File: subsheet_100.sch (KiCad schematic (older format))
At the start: 21 parts, among them U100 MC68000_PLCC_68_PHY, U100_DIP64 MC68000_DIP_64_SOCKET

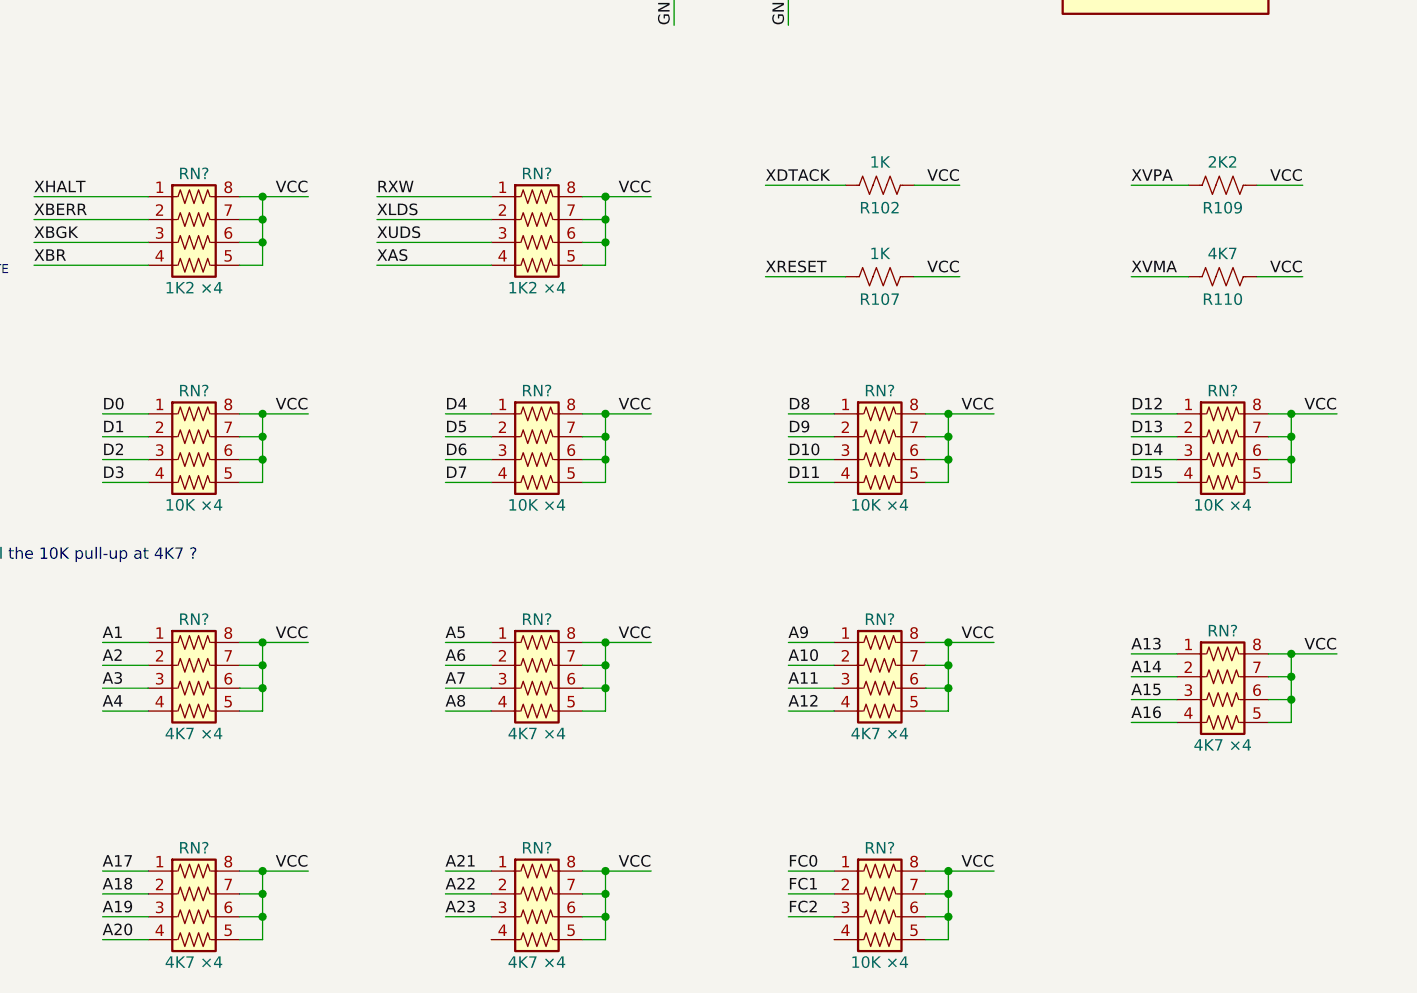
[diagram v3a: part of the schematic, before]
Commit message: annotate resistor networks and mark unused pins as unconnected
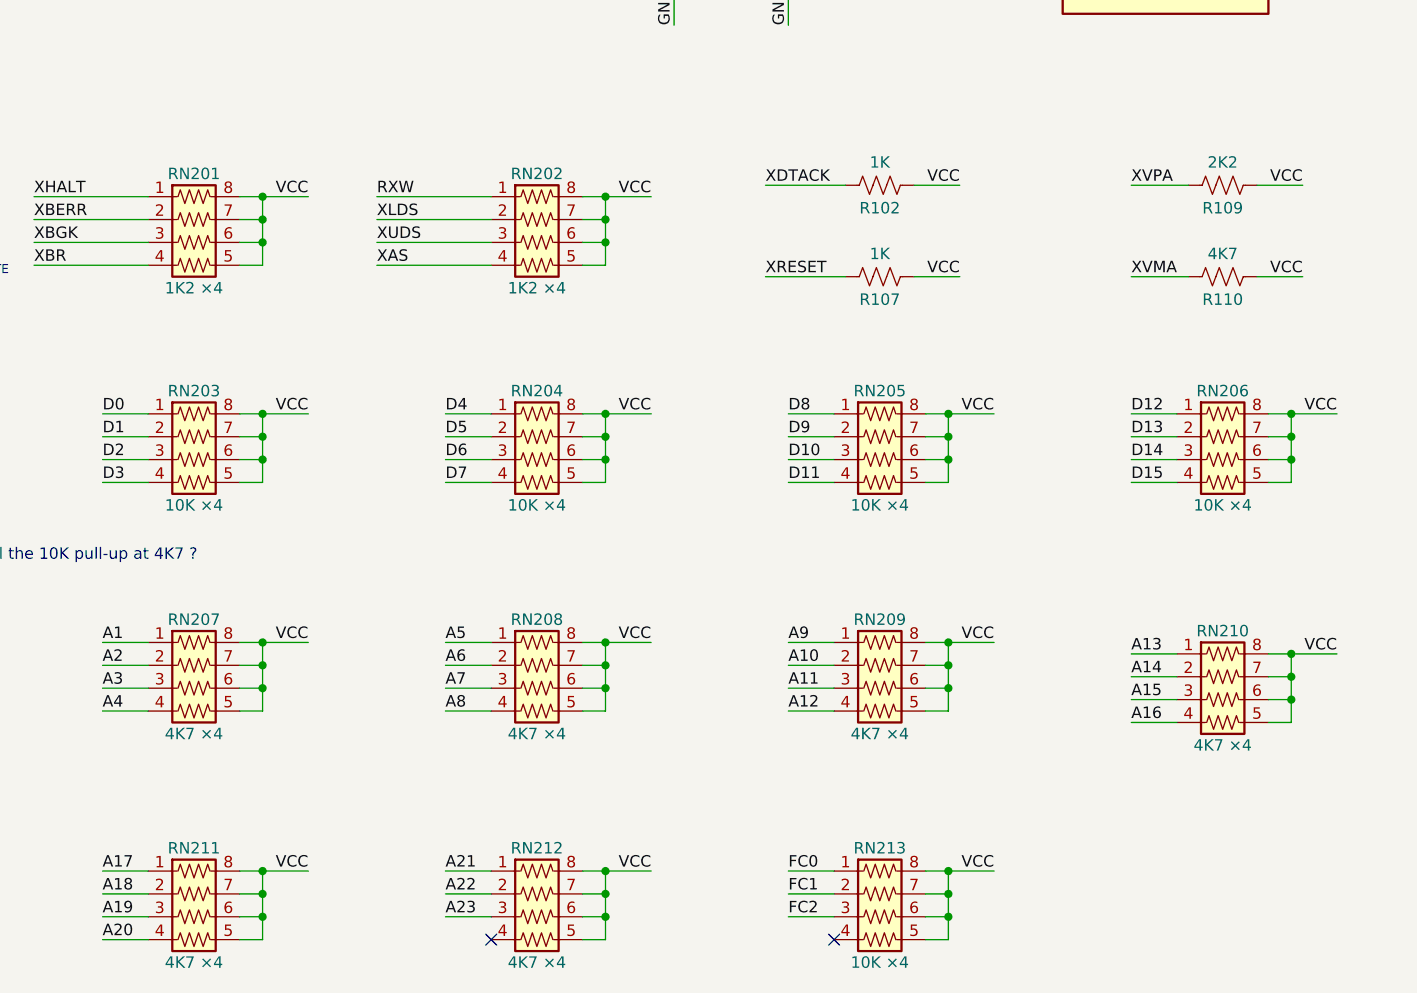
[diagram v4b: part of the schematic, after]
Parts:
- gave numbers to parts that had none: 13
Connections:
- no-connect marks 0 -> 2
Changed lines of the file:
@@
 XBGK when coming to \nBlitter is pulled-up\nwith 4K7, but in my STE\nit was not populated \nanyway (no external\nBlitter), so pulled-up \nwith 1K2 should be ok
 $Comp
-L custom_passives:R_Pack04_US RN?
+L custom_passives:R_Pack04_US RN201
 U 1 1 61B5A520
 P 2000 6250
-F 0 "RN?" V 1700 6250 50  0000 C CNN
+F 0 "RN201" V 1700 6250 50  0000 C CNN
 F 1 "1K2 ×4" V 2200 6250 50  0000 C CNN
 F 2 "" V 2275 6250 50  0001 C CNN
@@
 $EndComp
 $Comp
-L custom_passives:R_Pack04_US RN?
+L custom_passives:R_Pack04_US RN203
 U 1 1 61B5C554
 P 2000 7200
-F 0 "RN?" V 1700 7200 50  0000 C CNN
+F 0 "RN203" V 1700 7200 50  0000 C CNN
 F 1 "10K ×4" V 2200 7200 50  0000 C CNN
 F 2 "" V 2275 7200 50  0001 C CNN
@@
 $EndComp
 $Comp
-L custom_passives:R_Pack04_US RN?
+L custom_passives:R_Pack04_US RN202
 U 1 1 61B5F292
 P 3500 6250
-F 0 "RN?" V 3200 6250 50  0000 C CNN
+F 0 "RN202" V 3200 6250 50  0000 C CNN
 F 1 "1K2 ×4" V 3700 6250 50  0000 C CNN
 F 2 "" V 3775 6250 50  0001 C CNN
@@
 	3800 6150 3800 6050
 $Comp
-L custom_passives:R_Pack04_US RN?
+L custom_passives:R_Pack04_US RN204
 U 1 1 61BD00C3
 P 3500 7200
-F 0 "RN?" V 3200 7200 50  0000 C CNN
+F 0 "RN204" V 3200 7200 50  0000 C CNN
 F 1 "10K ×4" V 3700 7200 50  0000 C CNN
 F 2 "" V 3775 7200 50  0001 C CNN
@@
 $EndComp
 $Comp
-L custom_passives:R_Pack04_US RN?
+L custom_passives:R_Pack04_US RN205
 U 1 1 61BD08B3
 P 5000 7200
-F 0 "RN?" V 4700 7200 50  0000 C CNN
+F 0 "RN205" V 4700 7200 50  0000 C CNN
 F 1 "10K ×4" V 5200 7200 50  0000 C CNN
 F 2 "" V 5275 7200 50  0001 C CNN
@@
 $EndComp
 $Comp
-L custom_passives:R_Pack04_US RN?
+L custom_passives:R_Pack04_US RN206
 U 1 1 61BD1305
 P 6500 7200
-F 0 "RN?" V 6200 7200 50  0000 C CNN
+F 0 "RN206" V 6200 7200 50  0000 C CNN
 F 1 "10K ×4" V 6700 7200 50  0000 C CNN
 F 2 "" V 6775 7200 50  0001 C CNN
@@
 	6800 7100 6800 7000
 $Comp
-L custom_passives:R_Pack04_US RN?
+L custom_passives:R_Pack04_US RN207
 U 1 1 61CC273F
 P 2000 8200
-F 0 "RN?" V 1700 8200 50  0000 C CNN
+F 0 "RN207" V 1700 8200 50  0000 C CNN
 F 1 "4K7 ×4" V 2200 8200 50  0000 C CNN
 F 2 "" V 2275 8200 50  0001 C CNN
@@
 $EndComp
 $Comp
-L custom_passives:R_Pack04_US RN?
+L custom_passives:R_Pack04_US RN208
 U 1 1 61CDAA84
 P 3500 8200
-F 0 "RN?" V 3200 8200 50  0000 C CNN
+F 0 "RN208" V 3200 8200 50  0000 C CNN
 F 1 "4K7 ×4" V 3700 8200 50  0000 C CNN
 F 2 "" V 3775 8200 50  0001 C CNN
@@
 $EndComp
 $Comp
-L custom_passives:R_Pack04_US RN?
+L custom_passives:R_Pack04_US RN209
 U 1 1 61CDBA85
 P 5000 8200
-F 0 "RN?" V 4700 8200 50  0000 C CNN
+F 0 "RN209" V 4700 8200 50  0000 C CNN
 F 1 "4K7 ×4" V 5200 8200 50  0000 C CNN
 F 2 "" V 5275 8200 50  0001 C CNN
@@
 $EndComp
 $Comp
-L custom_passives:R_Pack04_US RN?
+L custom_passives:R_Pack04_US RN210
 U 1 1 61CDC731
 P 6500 8250
-F 0 "RN?" V 6200 8250 50  0000 C CNN
+F 0 "RN210" V 6200 8250 50  0000 C CNN
 F 1 "4K7 ×4" V 6700 8250 50  0000 C CNN
 F 2 "" V 6775 8250 50  0001 C CNN
@@
 $EndComp
 $Comp
-L custom_passives:R_Pack04_US RN?
+L custom_passives:R_Pack04_US RN211
 U 1 1 61D5A646
 P 2000 9200
-F 0 "RN?" V 1700 9200 50  0000 C CNN
+F 0 "RN211" V 1700 9200 50  0000 C CNN
 F 1 "4K7 ×4" V 2200 9200 50  0000 C CNN
 F 2 "" V 2275 9200 50  0001 C CNN
@@
 $EndComp
 $Comp
-L custom_passives:R_Pack04_US RN?
+L custom_passives:R_Pack04_US RN212
 U 1 1 61D5B85C
 P 3500 9200
-F 0 "RN?" V 3200 9200 50  0000 C CNN
+F 0 "RN212" V 3200 9200 50  0000 C CNN
 F 1 "4K7 ×4" V 3700 9200 50  0000 C CNN
 F 2 "" V 3775 9200 50  0001 C CNN
@@
 	3800 9100 3800 9000
 $Comp
-L custom_passives:R_Pack04_US RN?
+L custom_passives:R_Pack04_US RN213
 U 1 1 61ED1BB1
 P 5000 9200
-F 0 "RN?" V 4700 9200 50  0000 C CNN
+F 0 "RN213" V 4700 9200 50  0000 C CNN
 F 1 "10K ×4" V 5200 9200 50  0000 C CNN
 F 2 "" V 5275 9200 50  0001 C CNN
@@
 Text Notes 700  7650 0    50   ~ 0
 Maybe put all the 10K pull-up at 4K7 ?
+NoConn ~ 3300 9300
+NoConn ~ 4800 9300
 $EndSCHEMATC

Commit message: Resolves #7 : Assign SMD footprints to resistors pack
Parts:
- RN201, RN202, RN203, RN204, RN205, RN206, RN207, RN208, RN209, RN210, RN211, RN212, RN213: footprint (none) -> Resistor_SMD:R_Array_Convex_4x0603
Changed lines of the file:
@@
 F 0 "RN201" V 1700 6250 50  0000 C CNN
 F 1 "1K2 ×4" V 2200 6250 50  0000 C CNN
-F 2 "" V 2275 6250 50  0001 C CNN
+F 2 "Resistor_SMD:R_Array_Convex_4x0603" V 2275 6250 50  0001 C CNN
 F 3 "~" H 2000 6250 50  0001 C CNN
 	1    2000 6250
@@
 F 0 "RN203" V 1700 7200 50  0000 C CNN
 F 1 "10K ×4" V 2200 7200 50  0000 C CNN
-F 2 "" V 2275 7200 50  0001 C CNN
+F 2 "Resistor_SMD:R_Array_Convex_4x0603" V 2275 7200 50  0001 C CNN
 F 3 "~" H 2000 7200 50  0001 C CNN
 	1    2000 7200
@@
 F 0 "RN202" V 3200 6250 50  0000 C CNN
 F 1 "1K2 ×4" V 3700 6250 50  0000 C CNN
-F 2 "" V 3775 6250 50  0001 C CNN
+F 2 "Resistor_SMD:R_Array_Convex_4x0603" V 3775 6250 50  0001 C CNN
 F 3 "~" H 3500 6250 50  0001 C CNN
 	1    3500 6250
@@
 F 0 "RN204" V 3200 7200 50  0000 C CNN
 F 1 "10K ×4" V 3700 7200 50  0000 C CNN
-F 2 "" V 3775 7200 50  0001 C CNN
+F 2 "Resistor_SMD:R_Array_Convex_4x0603" V 3775 7200 50  0001 C CNN
 F 3 "~" H 3500 7200 50  0001 C CNN
 	1    3500 7200
@@
 F 0 "RN205" V 4700 7200 50  0000 C CNN
 F 1 "10K ×4" V 5200 7200 50  0000 C CNN
-F 2 "" V 5275 7200 50  0001 C CNN
+F 2 "Resistor_SMD:R_Array_Convex_4x0603" V 5275 7200 50  0001 C CNN
 F 3 "~" H 5000 7200 50  0001 C CNN
 	1    5000 7200
@@
 F 0 "RN206" V 6200 7200 50  0000 C CNN
 F 1 "10K ×4" V 6700 7200 50  0000 C CNN
-F 2 "" V 6775 7200 50  0001 C CNN
+F 2 "Resistor_SMD:R_Array_Convex_4x0603" V 6775 7200 50  0001 C CNN
 F 3 "~" H 6500 7200 50  0001 C CNN
 	1    6500 7200
@@
 F 0 "RN207" V 1700 8200 50  0000 C CNN
 F 1 "4K7 ×4" V 2200 8200 50  0000 C CNN
-F 2 "" V 2275 8200 50  0001 C CNN
+F 2 "Resistor_SMD:R_Array_Convex_4x0603" V 2275 8200 50  0001 C CNN
 F 3 "~" H 2000 8200 50  0001 C CNN
 	1    2000 8200
@@
 F 0 "RN208" V 3200 8200 50  0000 C CNN
 F 1 "4K7 ×4" V 3700 8200 50  0000 C CNN
-F 2 "" V 3775 8200 50  0001 C CNN
+F 2 "Resistor_SMD:R_Array_Convex_4x0603" V 3775 8200 50  0001 C CNN
 F 3 "~" H 3500 8200 50  0001 C CNN
 	1    3500 8200
@@
 F 0 "RN209" V 4700 8200 50  0000 C CNN
 F 1 "4K7 ×4" V 5200 8200 50  0000 C CNN
-F 2 "" V 5275 8200 50  0001 C CNN
+F 2 "Resistor_SMD:R_Array_Convex_4x0603" V 5275 8200 50  0001 C CNN
 F 3 "~" H 5000 8200 50  0001 C CNN
 	1    5000 8200
@@
 F 0 "RN210" V 6200 8250 50  0000 C CNN
 F 1 "4K7 ×4" V 6700 8250 50  0000 C CNN
-F 2 "" V 6775 8250 50  0001 C CNN
+F 2 "Resistor_SMD:R_Array_Convex_4x0603" V 6775 8250 50  0001 C CNN
 F 3 "~" H 6500 8250 50  0001 C CNN
 	1    6500 8250
@@
 F 0 "RN211" V 1700 9200 50  0000 C CNN
 F 1 "4K7 ×4" V 2200 9200 50  0000 C CNN
-F 2 "" V 2275 9200 50  0001 C CNN
+F 2 "Resistor_SMD:R_Array_Convex_4x0603" V 2275 9200 50  0001 C CNN
 F 3 "~" H 2000 9200 50  0001 C CNN
 	1    2000 9200
@@
 F 0 "RN212" V 3200 9200 50  0000 C CNN
 F 1 "4K7 ×4" V 3700 9200 50  0000 C CNN
-F 2 "" V 3775 9200 50  0001 C CNN
+F 2 "Resistor_SMD:R_Array_Convex_4x0603" V 3775 9200 50  0001 C CNN
 F 3 "~" H 3500 9200 50  0001 C CNN
 	1    3500 9200
@@
 F 0 "RN213" V 4700 9200 50  0000 C CNN
 F 1 "10K ×4" V 5200 9200 50  0000 C CNN
-F 2 "" V 5275 9200 50  0001 C CNN
+F 2 "Resistor_SMD:R_Array_Convex_4x0603" V 5275 9200 50  0001 C CNN
 F 3 "~" H 5000 9200 50  0001 C CNN
 	1    5000 9200
